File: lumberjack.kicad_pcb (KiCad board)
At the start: 2 copper layers, 284.7 x 94.2 mm, 163 parts, among them J1 USB, J2 AVR_ISP_6, J3 JST, J4 JST, SW1 RESET, SW2 BOOT, U1 ATMEGA328-PU, Y1 16MHz

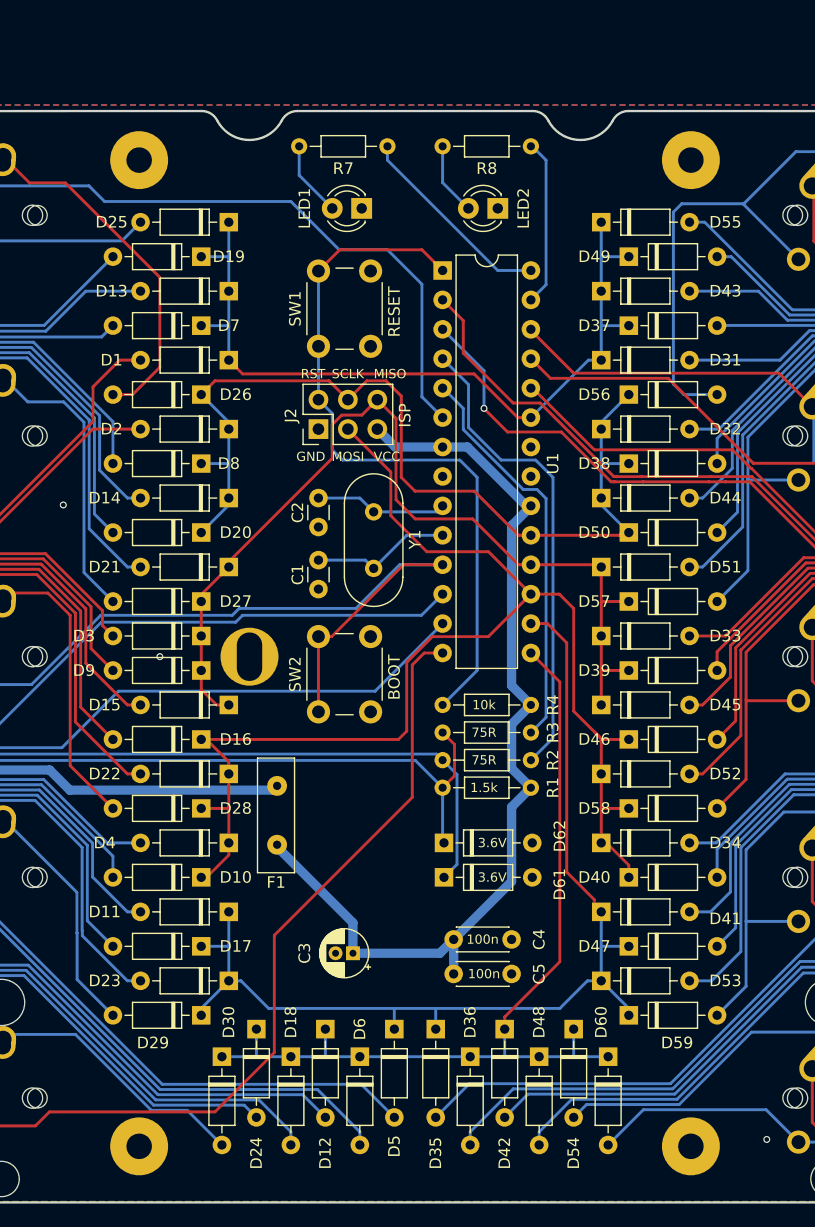
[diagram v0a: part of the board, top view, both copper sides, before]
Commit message: 修改丝印，增加屏幕插座
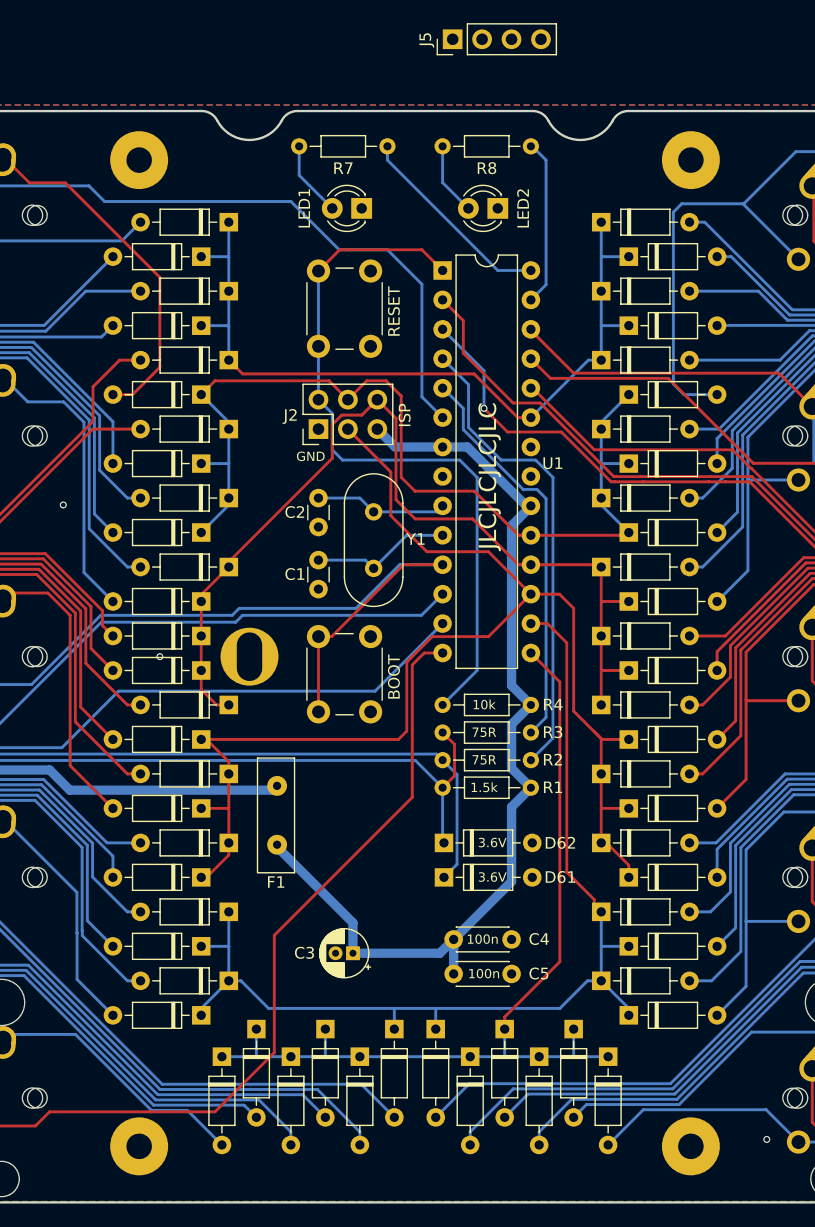
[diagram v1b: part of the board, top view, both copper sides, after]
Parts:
- added J5: Conn_01x04_Female, Connector_PinHeader_2.54mm:PinHeader_1x04_P2.54mm_Vertical, F.Cu at (155.7, 49.1)
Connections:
- U1 pad 27: /LED2 -> /SDA
- U1 pad 28: /LED1 -> /SCL
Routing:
- net /SCL: track 0.00 -> 17.5 mm
- net /LED1: track 17.5 -> 0.00 mm
- net /SDA: track 0.00 -> 14.4 mm
- net /LED2: track 14.4 -> 0.00 mm
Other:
- board text added: "JLCJLCJLCJLC"
- board text removed: "MISO"
- board text removed: "MOSI"
- board text removed: "RST"
- board text removed: "SCLK"
- board text removed: "VCC"
